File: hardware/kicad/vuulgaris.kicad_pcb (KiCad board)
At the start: 2 copper layers, 284.3 x 125 mm, 43 parts, among them J1 TFPUSH, J2 WQP-WQP518MA_WQP-PJ398SM, J3 WQP-WQP518MA_WQP-PJ398SM, J4 WQP-WQP518MA_WQP-PJ398SM, J5 WQP-WQP518MA_WQP-PJ398SM, J6 WQP-WQP518MA_WQP-PJ398SM, SW4 CPG151101S03, SW5 CPG151101S03, SW6 CPG151101S03, SW7 CPG151101S03, U1 ES_DAISY_PATCH_SM_REV1, U3 MCP23017-E_SO, U4 MCP23017-E_SO, U5 AMS1117-3.3, U6 AMS1117-3.3

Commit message: hardware: Daisy on the right wall for USB, jacks along the top edge
The Daisy is rotated 90 degrees hard against the right wall, putting its USB-C at
(282.5, 85.2), 1.8mm inside the edge. That reverses the recorded decision that USB
access meant unscrewing the module, and it costs no pins: DFU and USB MIDI device
both run on the module's own connector, so A8/A9 stay free as already decided.

Only the right wall works. USB, the D header and the C header are all on the same
long edge of the module, so whichever wall the USB faces the SD and CV face too.
The left is blocked by ENC0 and the MX cluster -- about 16mm clear against the
module's 68mm -- and the top 47mm is entirely panel controls.

The SD card is not user-accessible and that is accepted. The module occupies 68 of
the 77mm of clear height at that wall, so J1 cannot sit beside its own D header;
it is parked to the left at a 39.5mm run, rotated so the card slot faces open
board rather than the bottom wall 1.3mm away, where no card could have been
inserted at all.

Jacks: J6 dropped, so J2-J5 are the four 3.5mm CV/gate jacks, and J7-J10 are the
1/4" audio pairs. The 1/4" jacks sit along the top edge with their bushings at the
board edge and their bodies running 34mm inward, two of them under the OLED --
which is a module on standoffs, so only its holes matter, and those sit at its
corners and header. All 16 of their pins are deliberately unconnected: which
contact is tip, sleeve and switch is not established, and guessing it would be
inventing the pinout. J2-J5 are unwired for the same reason.

Schematic: 46 components, 160 connections, 58 nets, VERIFIED 160/160 with 0
unintended. Board: 0 overlapping flashes on F.Cu, 160 non-circular pads at the
orientation the library specifies.
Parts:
- removed J6: WQP-WQP518MA_WQP-PJ398SM, vuulgaris:CONN-TH_WQP-WQP518MA
- added J10: PJ-603_C41409498, vuulgaris:AUDIO-TH_PJ-603, F.Cu at (331.0, 74.5)
- added J7: PJ-603_C41409498, vuulgaris:AUDIO-TH_PJ-603, F.Cu at (270.5, 74.5)
- added J8: PJ-603_C41409498, vuulgaris:AUDIO-TH_PJ-603, F.Cu at (288.5, 74.5)
- added J9: PJ-603_C41409498, vuulgaris:AUDIO-TH_PJ-603, F.Cu at (313.0, 74.5)
- moved U1 143.5 mm to (363.5, 138.0), turned to 90 degrees
- moved R20 118.4 mm to (340.0, 108.0)
- moved R21 113.1 mm to (340.0, 114.0)
- moved J1 66.0 mm to (336.0, 150.0), turned to -90 degrees
- moved ENC1 3.75 mm to (118.1, 69.1)
- moved ENC10 3.75 mm to (212.1, 86.7)
- moved ENC2 3.75 mm to (118.1, 86.7)
- moved ENC3 3.75 mm to (140.1, 69.1)
- moved ENC4 3.75 mm to (140.1, 86.7)
- moved ENC5 3.75 mm to (162.1, 69.1)
- moved ENC6 3.75 mm to (162.1, 86.7)
- moved ENC7 3.75 mm to (184.1, 69.1)
- moved ENC8 3.75 mm to (184.1, 86.7)
- moved ENC9 3.75 mm to (212.1, 69.1)
- moved ENC0 0.20 mm to (126.6, 119.7)

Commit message: hardware: jacks on the back, CV evenly spaced between the encoders
All eight edge jacks are now on B.Cu with their barrels at the top edge. The 1/4"
pairs cluster on the right under the OLED at 16mm pitch; the four CV/gate jacks
sit between the encoder columns on the encoders' own 22mm pitch, so their spacing
is exactly equal.

Judging them by BODY width said this was impossible: PJ-376 is 9.2mm wide and the
encoder gaps are 7.3mm. But at -90 degrees on the back the three pads all sit on
the origin's X axis and run along Y, so the copper is only 3.10mm wide. Every jack
clears the encoder pads either side by 2.10mm. What matters between a back-side
part and a front-side one is the holes, not the outlines.

The bodies do overlap the encoder footprints in plan view. That is accepted: the
encoders are on the opposite face, and the only physical conflict is their pin
tails, which need clipping flush.

Flipping in Pcbnew mirrored every X coordinate about x=143.415, which threw J7,
J9 and J10 into the encoder bank with their pads colliding with ENC5, ENC6, ENC8,
ENC9 and ENC10. All eight repositioned from scratch afterwards.

place.py's pad-orientation check is now mirror-aware: mirroring negates a pad's
relative angle, so a back-side footprint is fp_angle MINUS the library angle. It
was reporting 12 false failures against the flipped jacks before this.

Verified: 156 non-circular pads at the library orientation, 0 pad overlaps, all 20
panel parts on their holes, and 0 overlapping flashes across both copper layers in
the exported Gerbers.
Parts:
- J10, J7, J8, J9: moved to B.Cu
- J2, J3, J4, J5: value WQP-WQP518MA_WQP-PJ398SM -> PJ-376; footprint vuulgaris:CONN-TH_WQP-WQP518MA -> vuulgaris:AUDIO-TH_PJ-376; moved to B.Cu
- moved J5 118.0 mm to (195.2, 62.5), turned to -90 degrees
- moved J4 114.5 mm to (173.2, 62.5), turned to -90 degrees
- moved J3 111.5 mm to (151.2, 62.5), turned to -90 degrees
- moved J2 109.0 mm to (129.2, 62.5), turned to -90 degrees
- moved J7 43.1 mm to (313.6, 74.5)
- moved J8 41.1 mm to (329.6, 74.5)
- moved J9 32.6 mm to (345.6, 74.5)
- moved J10 30.6 mm to (361.6, 74.5)

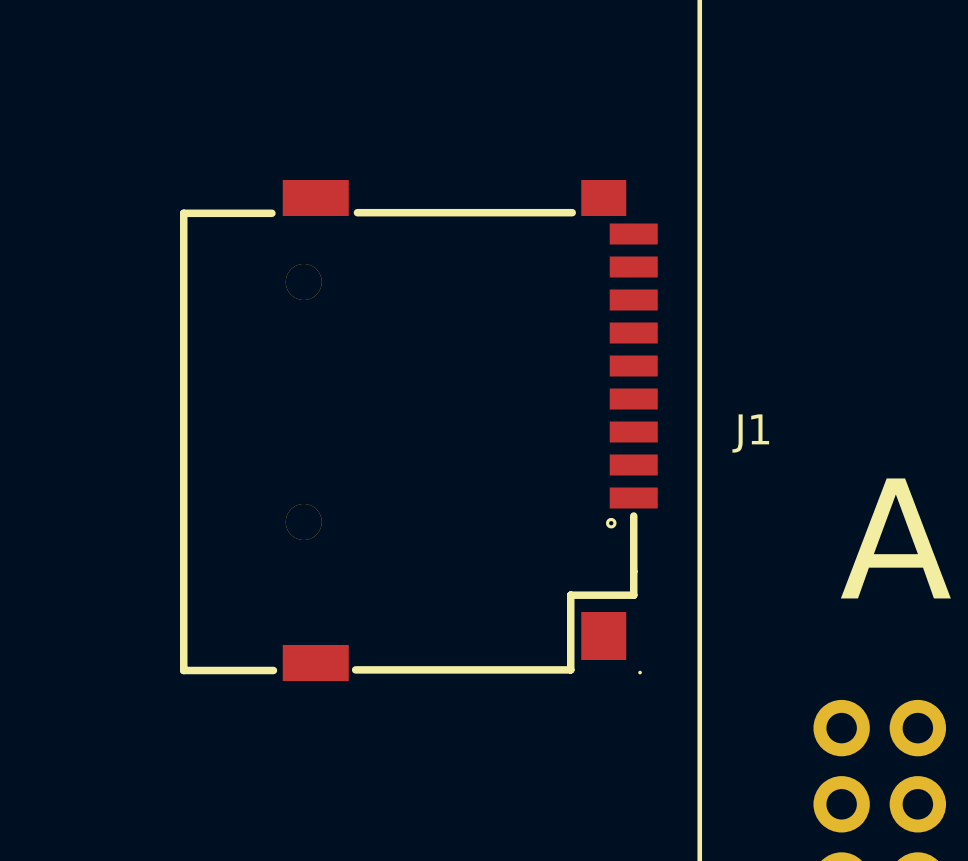
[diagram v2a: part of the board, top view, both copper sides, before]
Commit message: hardware: SD card to the back as well
J1 moves to B.Cu, rotated 90 so that after mirroring the card slot still faces
left into open board rather than at the Daisy 2.5mm away. Position unchanged at
(236, 100).

Flipping in the file means three things, not one: every F.* layer token becomes
B.* (103 of them here), and mirroring negates each pad's relative angle, so the
absolute angle is fp_angle MINUS the library angle. The local pad coordinates are
NOT rewritten -- KiCad stores them unmirrored and applies the mirror when it
renders, which is why the earlier flipped jacks still read as their library
coordinates.

Verified four ways: no F.* tokens left in the block, 156 non-circular pads at the
orientation the library specifies, 0 overlapping flashes on either copper layer,
and the SD contacts still 0.400mm apart with a correctly rotated R,1.6X0.7
aperture. The flash counts moving 13 from F.Cu to B.Cu match J1's 13 SMD pads
exactly, which is an independent check that the layer rewrite was complete.
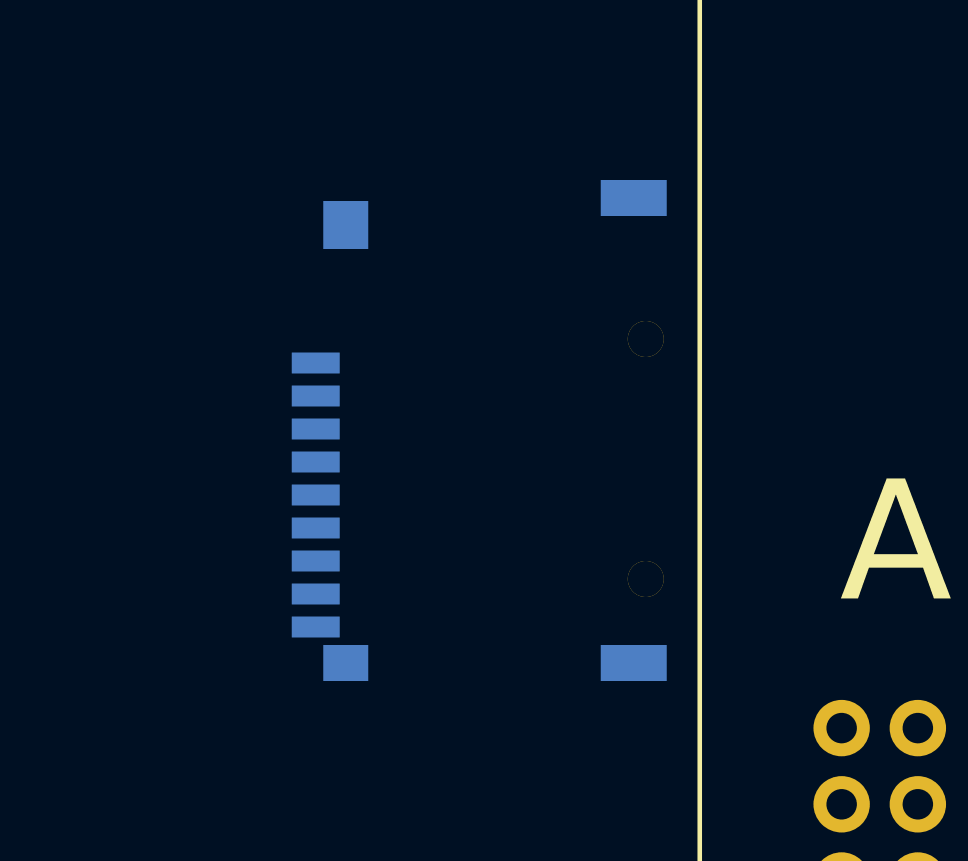
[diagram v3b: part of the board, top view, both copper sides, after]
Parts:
- J1: moved to B.Cu
- turned J1 to 90 degrees

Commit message: hardware: bring every jack forward so the barrels reach through the wall
The barrels were stopping at board y +0.50 -- half a millimetre INSIDE the board
edge, 7.5mm short of daylight. Nothing would have plugged in.

Geometry, board coordinates: edge at y 0, a 1.0mm assembly gap, then 6.0mm of
wall, so the outer face is y -7.00.

  J2-J5   origin y  5.00   barrel tip -7.00   flush with the outer face
  J7-J10  origin y 15.05   barrel tip -9.00   2.00mm proud

The 1/4" jacks have room to spare and could reach 8.20mm proud. The 3.5mm jacks
are at their limit: PJ-376's barrel is 12.00mm from origin to tip while its pads
reach 4.30mm the other way, so flush is the most it can do without walking the
pads off the board. They therefore cannot be nutted as drawn -- see the enclosure
TODO in design-state 11, which records counterboring the wall to 3mm at those four
spots as the fix, and why closing the 1mm gap was rejected instead.

Also re-spaced the 1/4" cluster to clear the OLED's mounting hardware. J7 and J10
sat 1.30 and 1.40mm from those pads; an M3 nut extends about 1.5mm past a 3.3mm
pad, so both would have fouled a fastener on the back face. Now 3.00mm each, with
the cluster inside 208.30..267.00 at 0.90mm between bodies.

That class of clash is invisible to every check here -- a screw head on a jack
body is neither a pad overlap nor a flash overlap. Same category as the encoder
pin tails over the CV jack bodies and the Daisy's standoff over the SD socket.

Verified: 156 non-circular pads at library orientation, 0 pad overlaps, all 20
panel parts on their holes, nothing outside the board outline.
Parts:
- moved J7 9.65 mm to (315.3, 65.0)
- moved J10 9.63 mm to (360.0, 65.0)
- moved J8 9.52 mm to (330.2, 65.0)
- moved J9 9.51 mm to (345.1, 65.0)
- moved J2 7.50 mm to (129.2, 55.0)
- moved J3 7.50 mm to (151.2, 55.0)
- moved J4 7.50 mm to (173.2, 55.0)
- moved J5 7.50 mm to (195.2, 55.0)
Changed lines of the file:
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@@
   )
   (footprint "vuulgaris:AUDIO-TH_PJ-376" (layer "B.Cu")
-    (at 173.15 62.5 -90)
+    (at 173.15 55.0 -90)
     (property "Sheetfile" "vuulgaris.kicad_sch")
     (property "Sheetname" "")
@@
   )
   (footprint "vuulgaris:AUDIO-TH_PJ-376" (layer "B.Cu")
-    (at 151.15 62.5 -90)
+    (at 151.15 55.0 -90)
     (property "Sheetfile" "vuulgaris.kicad_sch")
     (property "Sheetname" "")
@@
   )
   (footprint "vuulgaris:AUDIO-TH_PJ-376" (layer "B.Cu")
-    (at 129.15 62.5 -90)
+    (at 129.15 55.0 -90)
     (property "Sheetfile" "vuulgaris.kicad_sch")
     (property "Sheetname" "")
@@
   )
   (footprint "vuulgaris:AUDIO-TH_PJ-376" (layer "B.Cu")
-    (at 195.15 62.5 -90)
+    (at 195.15 55.0 -90)
     (property "Sheetfile" "vuulgaris.kicad_sch")
     (property "Sheetname" "")
@@
   )
   (footprint "vuulgaris:AUDIO-TH_PJ-603" (layer "B.Cu")
-    (at 313.6 74.55 -90)
+    (at 315.3 65.05 -90)
     (property "Sheetfile" "vuulgaris.kicad_sch")
     (property "Sheetname" "")
@@
   )
   (footprint "vuulgaris:AUDIO-TH_PJ-603" (layer "B.Cu")
-    (at 361.6 74.55 -90)
+    (at 360.0 65.05 -90)
     (property "Sheetfile" "vuulgaris.kicad_sch")
     (property "Sheetname" "")
@@
   )
   (footprint "vuulgaris:AUDIO-TH_PJ-603" (layer "B.Cu")
-    (at 345.6 74.55 -90)
+    (at 345.1 65.05 -90)
     (property "Sheetfile" "vuulgaris.kicad_sch")
     (property "Sheetname" "")
@@
   )
   (footprint "vuulgaris:AUDIO-TH_PJ-603" (layer "B.Cu")
-    (at 329.6 74.55 -90)
+    (at 330.2 65.05 -90)
     (property "Sheetfile" "vuulgaris.kicad_sch")
     (property "Sheetname" "")

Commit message: hardware: arrange the support parts by what they actually serve
J1 first: its body sat 0.91mm from the Daisy's A header, whose through-hole pins
protrude to the back face where J1 now lives. Moved up 8mm -- clearance 8.91mm to
the body, 10.65mm pad to pad -- for 3.2mm on the worst SD trace (39.50 -> 42.72).

Then everything that is not panel-facing, placed from the netlist rather than by
eye. Two rails leave U1.A6:

  P5V --+-- FB1 -- C24 -- U5 -- C21, C20 --> DS1.2
        +-- FB2 -- C25 -- U6 -- C23, C22 --> the faceplate PCB (no consumer yet)

Both LDOs sit with their input from the right and their TAB facing the load: on a
SOT-223 the tab is Vout and sits opposite the input pin, so the chain runs through
the part rather than doubling back. The OLED rail is directly under DS1 so the
regulated side is the short one.

  FB1 -> C24 input cap      8.0mm      C24 -> U5 Vin       3.8mm
  U5 tab -> C21 100nF       3.4mm      U5 tab -> C20 10uF 10.0mm
  U5 tab -> DS1.2           22.4mm

C23 was on the wrong side of the MSP rail: C22 is 10uF and C23 is 100nF, but C22
was nearer the output. The small ceramic has to be closest -- it is the
high-frequency decoupler and the bulk cap can sit beyond it. Swapped, so both
rails now read 100nF then 10uF outward from the tab.

Expanders go under the encoders they serve: U3 at x51 under ENC1-8, U4 at x105
under ENC9/10, each with its 100nF 3.8mm from pin 9. U4's buttons are 104mm away
at worst, which is fine -- they are switch closures to ground. The I2C pull-ups
stay at the master end beside U1's B header, 13-16mm from B7/B8; the bus then runs
181mm to U3, which at 400kHz with 2.2k is about 90ns of rise time against the
300ns the spec allows.

Verified: 156 non-circular pads at library orientation, 0 pad overlaps, no
same-face body overlaps, all 20 panel parts on their holes, and 0 overlapping
flashes on either copper layer.
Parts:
- moved FB2 130.4 mm to (285.0, 155.0)
- moved C25 124.0 mm to (279.0, 155.0)
- moved U6 105.5 mm to (272.0, 155.0)
- moved C23 88.1 mm to (266.0, 155.0)
- moved C22 82.6 mm to (260.0, 155.0)
- moved FB1 26.2 mm to (322.0, 106.0)
- moved C20 20.2 mm to (297.0, 106.0)
- moved C21 20.2 mm to (303.0, 106.0)
- moved C24 20.2 mm to (316.0, 106.0)
- moved U4 15.3 mm to (205.0, 105.0)
- moved C27 15.1 mm to (205.0, 113.0)
- moved J1 8.00 mm to (336.0, 142.0)
- moved U3 6.71 mm to (151.0, 105.0)
- moved C26 6.32 mm to (151.0, 113.0)
- moved U5 3.61 mm to (309.0, 106.0)
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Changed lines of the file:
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@@
   )
   (footprint "vuulgaris:R0402" (layer "F.Cu")
-    (at 340.0 114.0)
+    (at 338.0 114.0)
     (descr "2.2KΩ (2201) ±1%")
     (property "Sheetfile" "vuulgaris.kicad_sch")
@@
   )
   (footprint "vuulgaris:R0805" (layer "F.Cu")
-    (at 296.0 103.0)
+    (at 322.0 106.0)
     (property "Sheetfile" "vuulgaris.kicad_sch")
     (property "Sheetname" "")
@@
   )
   (footprint "vuulgaris:R0402" (layer "F.Cu")
-    (at 340.0 108.0)
+    (at 338.0 108.0)
     (descr "2.2KΩ (2201) ±1%")
     (property "Sheetfile" "vuulgaris.kicad_sch")
@@
   )
   (footprint "vuulgaris:SOT-223-3_L6.5-W3.4-P2.30-LS7.0-BR" (layer "F.Cu")
-    (at 307.0 103.0)
+    (at 309.0 106.0)
     (property "Sheetfile" "vuulgaris.kicad_sch")
     (property "Sheetname" "")
@@
   )
   (footprint "vuulgaris:C0805" (layer "F.Cu")
-    (at 317.0 103.0)
+    (at 297.0 106.0)
     (descr "10uF (106) ±10% 25V")
     (property "Sheetfile" "vuulgaris.kicad_sch")
@@
   )
   (footprint "vuulgaris:SOT-223-3_L6.5-W3.4-P2.30-LS7.0-BR" (layer "F.Cu")
-    (at 167.0 145.0)
+    (at 272.0 155.0)
     (property "Sheetfile" "vuulgaris.kicad_sch")
     (property "Sheetname" "")
@@
   )
   (footprint "vuulgaris:SOIC-28_L18.0-W7.5-P1.27-LS10.3-BL" (layer "F.Cu")
-    (at 145.0 102.0)
+    (at 151.0 105.0)
     (property "Sheetfile" "vuulgaris.kicad_sch")
     (property "Sheetname" "")
@@
   )
   (footprint "vuulgaris:C0402" (layer "F.Cu")
-    (at 190.0 111.0)
+    (at 205.0 113.0)
     (descr "100nF (104) ±10% 16V")
     (property "Sheetfile" "vuulgaris.kicad_sch")
@@
   )
   (footprint "vuulgaris:C0402" (layer "F.Cu")
-    (at 145.0 111.0)
+    (at 151.0 113.0)
     (descr "100nF (104) ±10% 16V")
     (property "Sheetfile" "vuulgaris.kicad_sch")
@@
   )
   (footprint "vuulgaris:R0805" (layer "F.Cu")
-    (at 155.0 145.0)
+    (at 285.0 155.0)
     (property "Sheetfile" "vuulgaris.kicad_sch")
     (property "Sheetname" "")
@@
   )
   (footprint "vuulgaris:C0805" (layer "F.Cu")
-    (at 155.0 152.0)
+    (at 279.0 155.0)
     (descr "10uF (106) ±10% 25V")
     (property "Sheetfile" "vuulgaris.kicad_sch")
@@
   )
   (footprint "vuulgaris:C0402" (layer "F.Cu")
-    (at 178.0 152.0)
+    (at 266.0 155.0)
     (descr "100nF (104) ±10% 16V")
     (property "Sheetfile" "vuulgaris.kicad_sch")
@@
   )
   (footprint "vuulgaris:C0402" (layer "F.Cu")
-    (at 323.0 109.0)
+    (at 303.0 106.0)
     (descr "100nF (104) ±10% 16V")
     (property "Sheetfile" "vuulgaris.kicad_sch")
@@
   )
   (footprint "vuulgaris:SOIC-28_L18.0-W7.5-P1.27-LS10.3-BL" (layer "F.Cu")
-    (at 190.0 102.0)
+    (at 205.0 105.0)
     (property "Sheetfile" "vuulgaris.kicad_sch")
     (property "Sheetname" "")
@@
   )
   (footprint "vuulgaris:TF-SMD_TF-PUSH" (layer "B.Cu")
-    (at 336.0 150.0 90)
+    (at 336.0 142.0 90)
     (property "Sheetfile" "vuulgaris.kicad_sch")
     (property "Sheetname" "")
@@
   )
   (footprint "vuulgaris:C0805" (layer "F.Cu")
-    (at 296.0 109.0)
+    (at 316.0 106.0)
     (descr "10uF (106) ±10% 25V")
     (property "Sheetfile" "vuulgaris.kicad_sch")
@@
   )
   (footprint "vuulgaris:C0805" (layer "F.Cu")
-    (at 178.0 145.0)
+    (at 260.0 155.0)
     (descr "10uF (106) ±10% 25V")
     (property "Sheetfile" "vuulgaris.kicad_sch")
